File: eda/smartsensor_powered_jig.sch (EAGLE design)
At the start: 7 parts, among them J2 AVR_SPI_PRG_6PTH

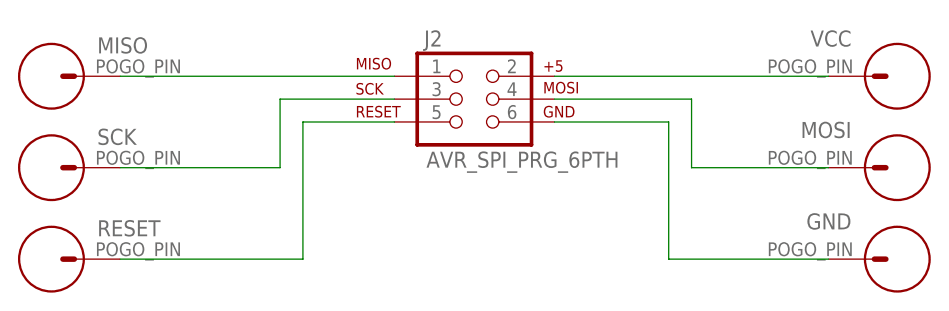
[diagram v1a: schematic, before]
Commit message: Ribboncable pinout fixed.
On battery_buzzer, smartsensor, and smartsensorPowered.
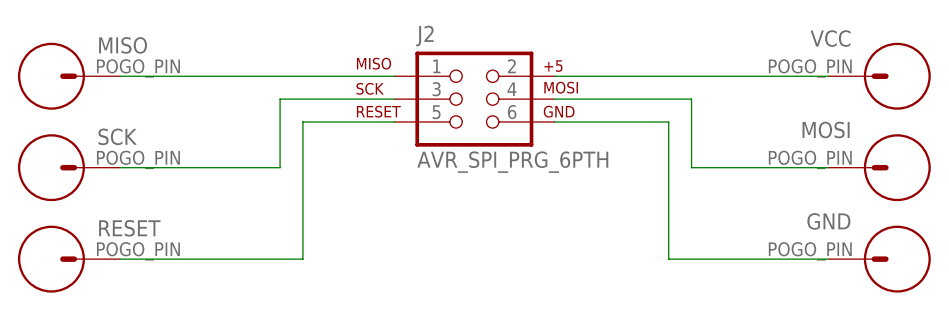
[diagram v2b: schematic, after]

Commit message: All jigs probe vias accessible after populating.
Also changed "VCC" signal name on jigs to "5V" to match boards.
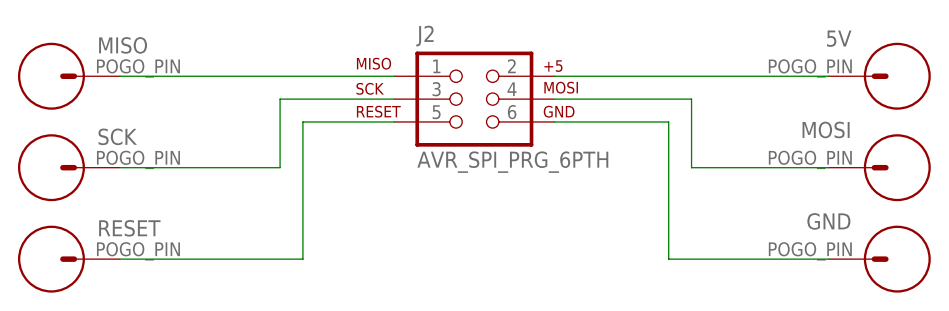
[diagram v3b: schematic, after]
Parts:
- renumbered VCC to 5V
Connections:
- net VCC renamed 5V
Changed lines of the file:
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@@
 <part name="SCK" library="pie" deviceset="POGO_PIN" device=""/>
 <part name="RESET" library="pie" deviceset="POGO_PIN" device=""/>
-<part name="VCC" library="pie" deviceset="POGO_PIN" device=""/>
+<part name="5V" library="pie" deviceset="POGO_PIN" device=""/>
 <part name="MOSI" library="pie" deviceset="POGO_PIN" device=""/>
 <part name="GND" library="pie" deviceset="POGO_PIN" device=""/>
@@
 <instance part="SCK" gate="G$1" x="76.2" y="104.14"/>
 <instance part="RESET" gate="G$1" x="76.2" y="93.98"/>
-<instance part="VCC" gate="G$1" x="170.18" y="114.3" smashed="yes" rot="R180">
+<instance part="5V" gate="G$1" x="170.18" y="114.3" smashed="yes" rot="R180">
 <attribute name="NAME" x="165.1" y="119.38" size="1.778" layer="95" rot="R180"/>
 <attribute name="VALUE" x="165.1" y="118.11" size="1.778" layer="96" rot="R180"/>
@@
 </segment>
 </net>
-<net name="VCC" class="0">
+<net name="5V" class="0">
 <segment>
 <pinref part="J2" gate="G$1" pin="2"/>
-<pinref part="VCC" gate="G$1" pin="P$1"/>
+<pinref part="5V" gate="G$1" pin="P$1"/>
 <wire x1="132.08" y1="114.3" x2="162.56" y2="114.3" width="0.1524" layer="91"/>
 </segment>
